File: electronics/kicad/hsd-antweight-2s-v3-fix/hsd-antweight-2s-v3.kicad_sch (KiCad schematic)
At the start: 13 parts, among them J10 ACCESSORY_POWER, J2 ESP32-C3_RIGHT, J4 BATTERY_2S_7V4, J5 MOTOR_LEFT, J6 MOTOR_RIGHT, J9 ESP32_RIGHT_BREAKOUT, SW1 MAIN_POWER, U1 ESP32-C3_LEFT, U2 DRV8833_BREAKOUT, U3 5V_BUCK_BOOST

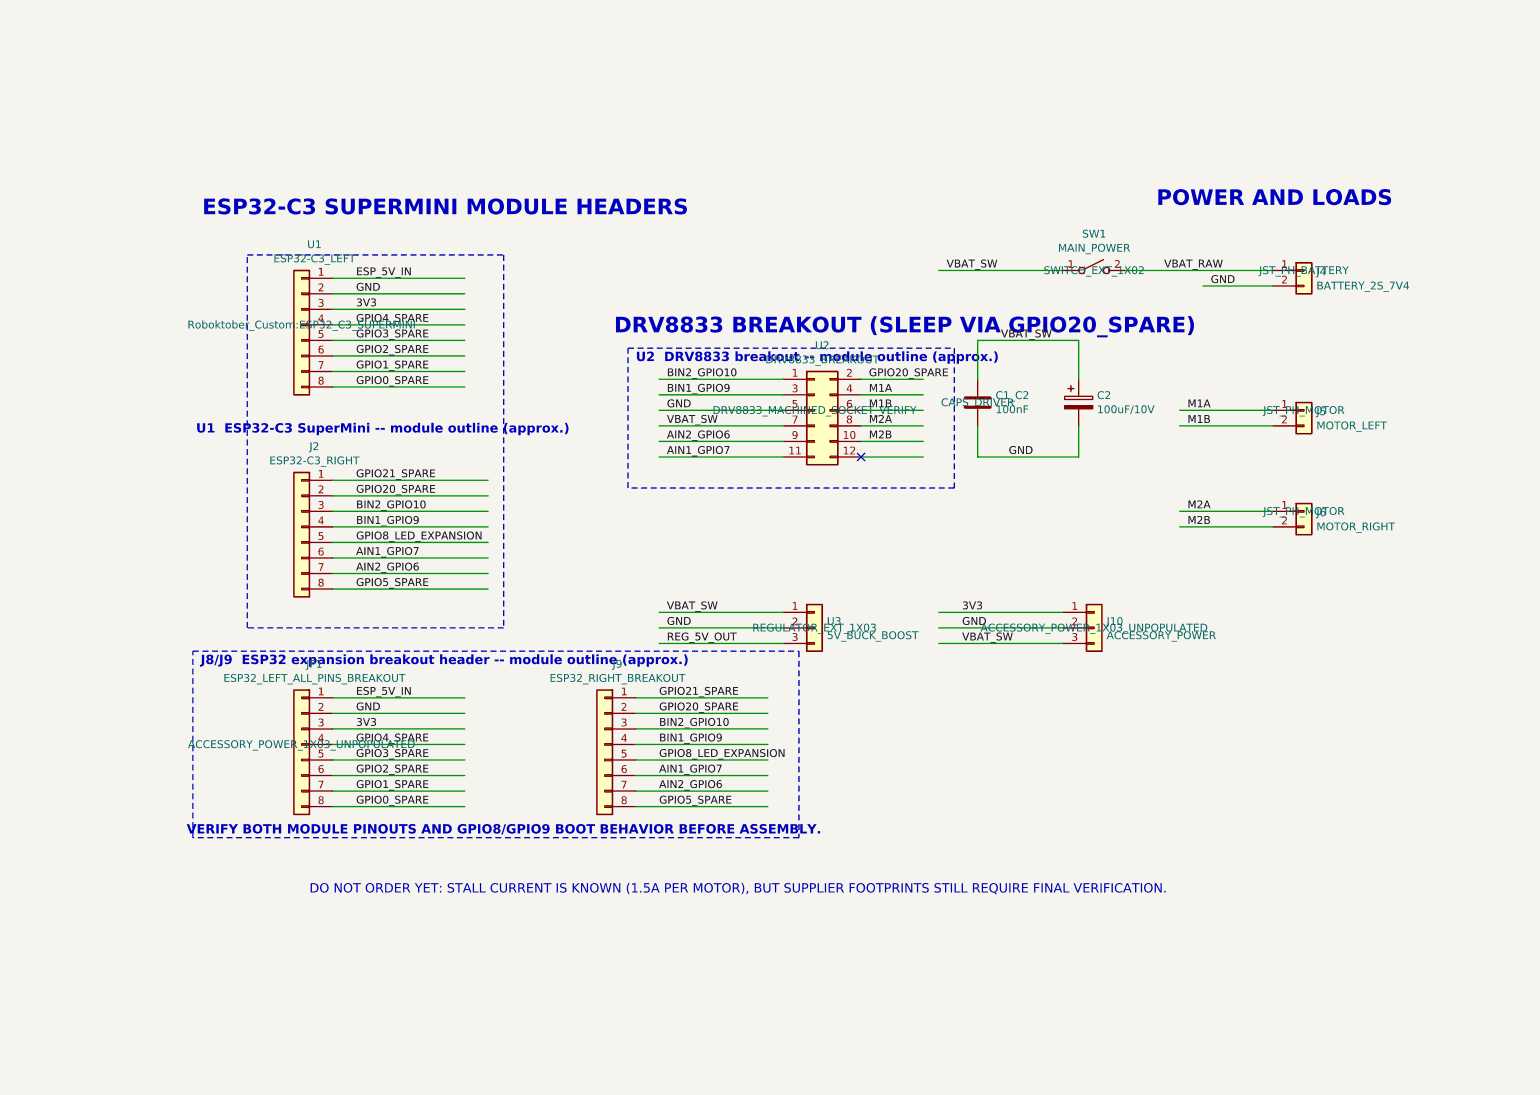
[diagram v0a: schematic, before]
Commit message: Align Wallie design notes with 1S default power architecture
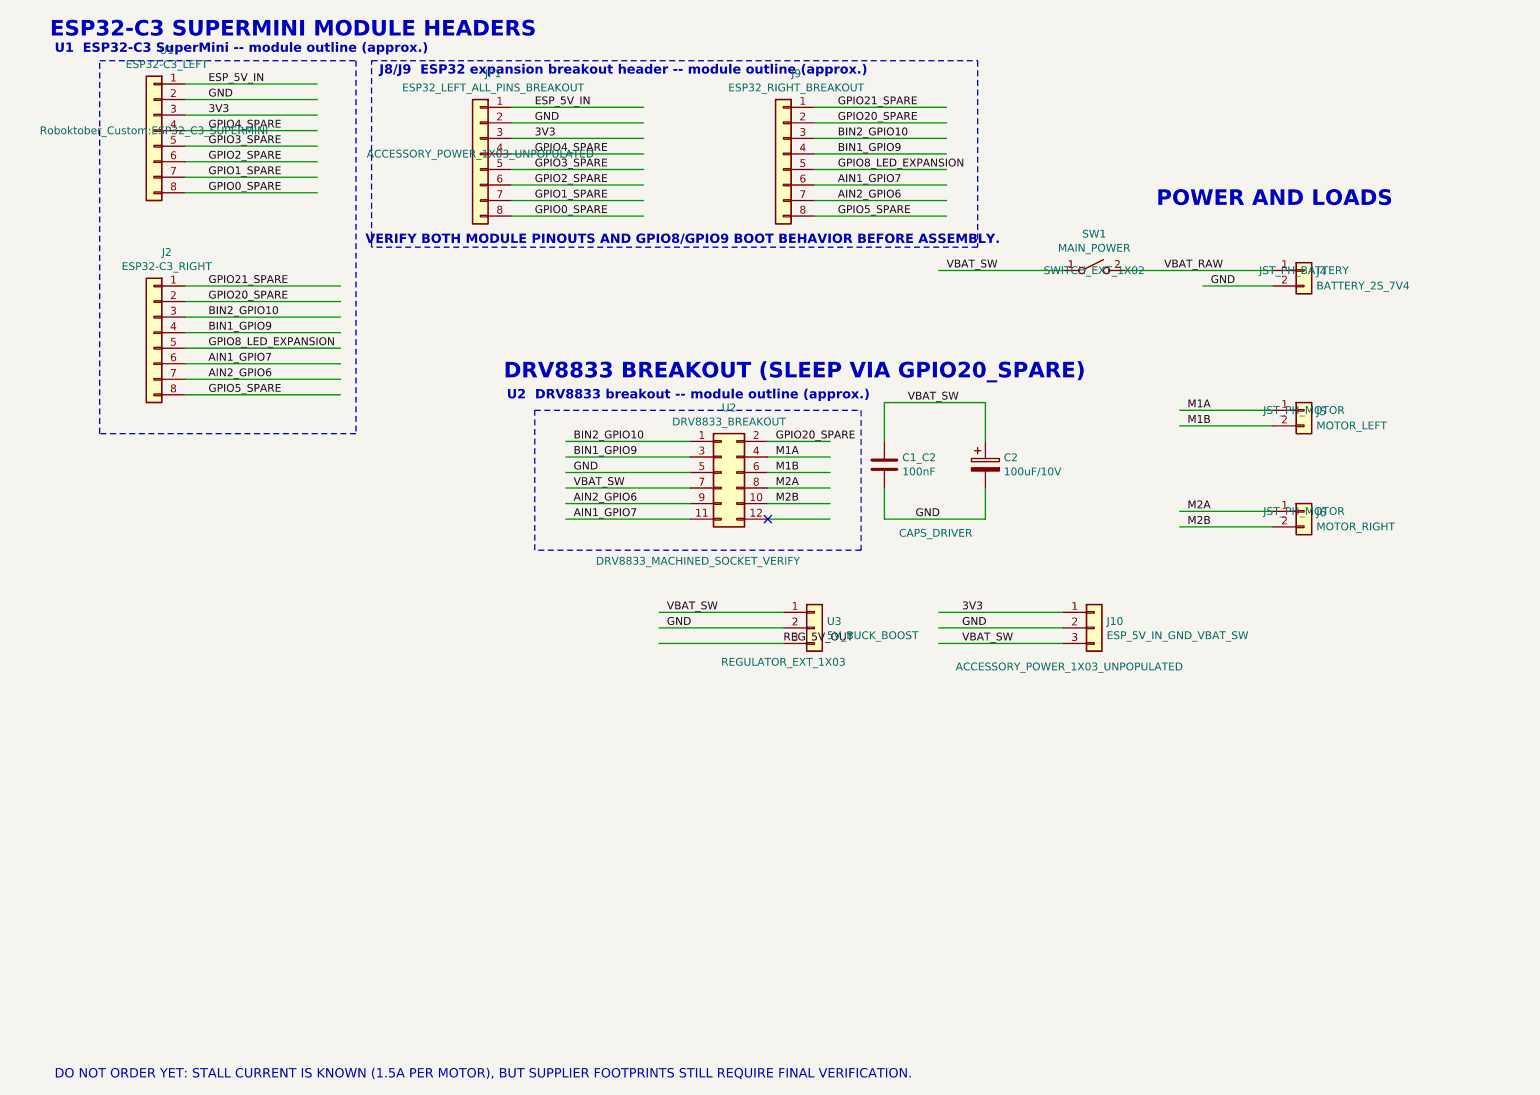
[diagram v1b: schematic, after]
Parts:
- J10: value ACCESSORY_POWER -> ESP_5V_IN_GND_VBAT_SW
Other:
- moved on the sheet: C1_C2, C2, J2, J9, JP1, U1, U2

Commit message: Fix PCB DRC: power trace width and silkscreen overlap
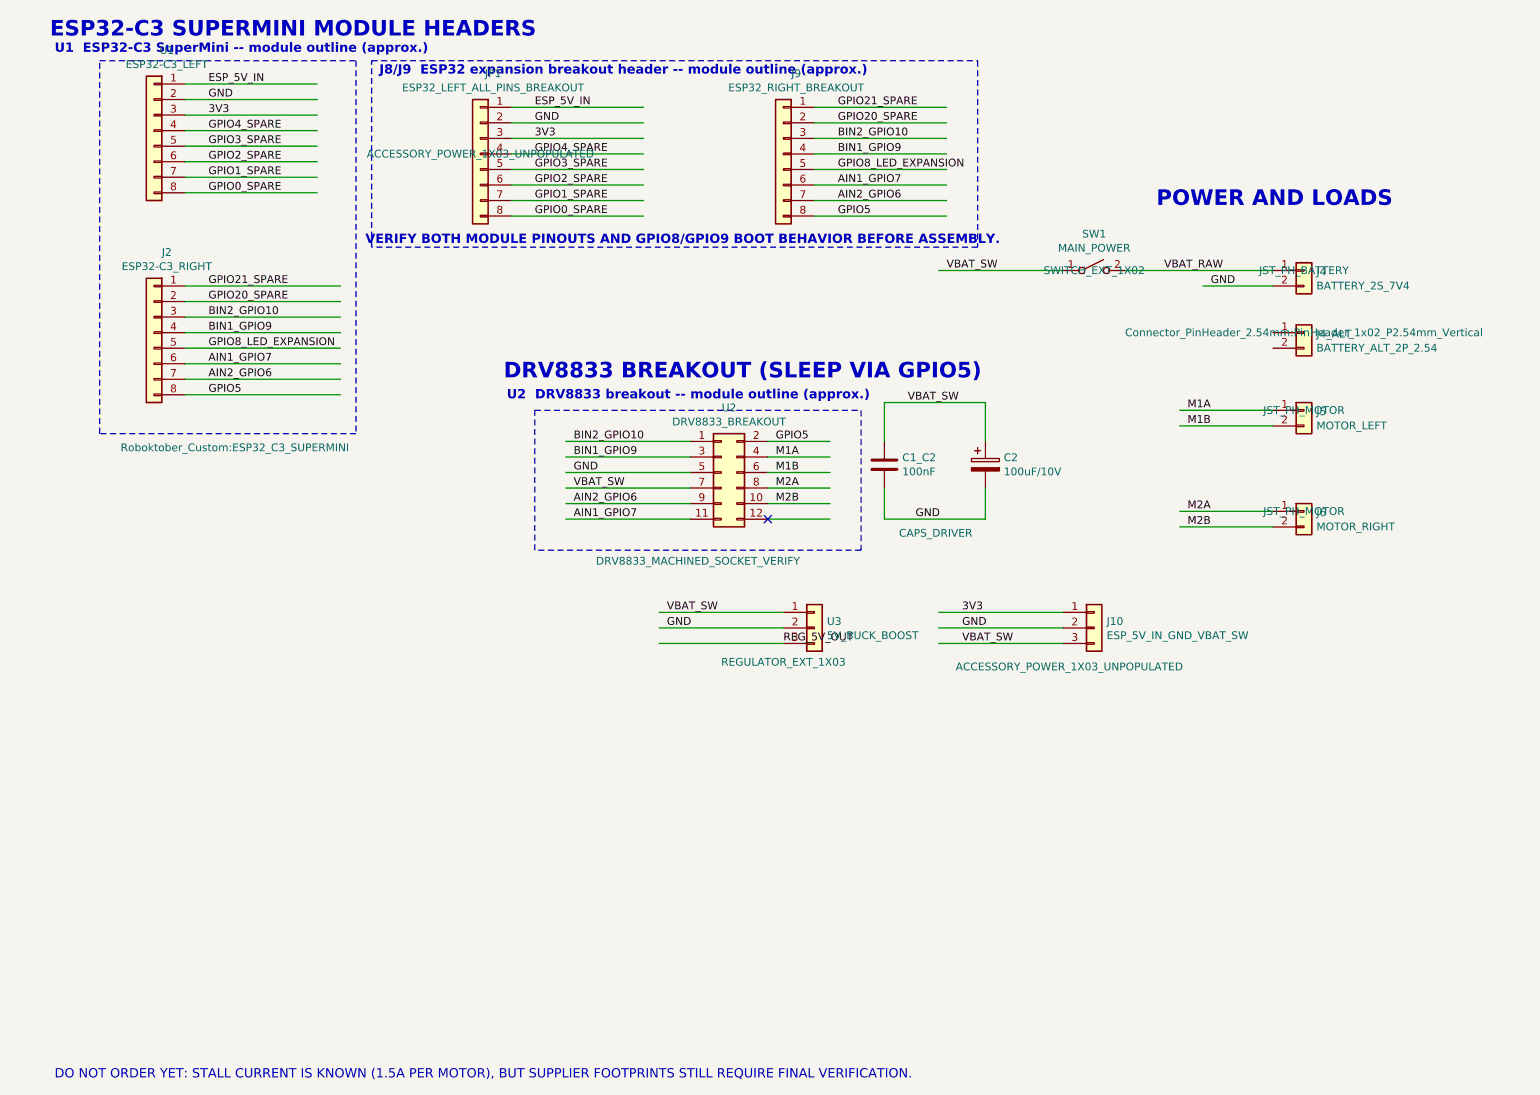
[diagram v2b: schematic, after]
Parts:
- added J4_ALT: BATTERY_ALT_2P_2.54, Connector_PinHeader_2.54mm:PinHeader_1x02_P2.54mm_Vertical, symbol Connector_Generic:Conn_01x02
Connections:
- net GPIO20_SPARE: no longer U2.2 (Pin_2)
- net GPIO5_SPARE renamed GPIO5
- net GPIO5: now also U2.2 (Pin_2)
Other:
- note added: "DRV8833 BREAKOUT (SLEEP VIA GPIO5)"
- note removed: "DRV8833 BREAKOUT (SLEEP VIA GPIO20_SPARE)"
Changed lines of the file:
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@@
 		(rev "3.0")
 		(company "Hackerspace Drenthe")
-		(comment 1 "ESP32-C3 SuperMini + DRV8833 carrier (nSLEEP wired to GPIO20_SPARE)")
+		(comment 1 "ESP32-C3 SuperMini + DRV8833 carrier (nSLEEP wired to GPIO5)")
 		(comment 2 "N20 600rpm measured max 1.5A per motor (3.0A combined)")
 	)
@@
 		)
 	)
-	(text "DRV8833 BREAKOUT (SLEEP VIA GPIO20_SPARE)"
+	(text "DRV8833 BREAKOUT (SLEEP VIA GPIO5)"
 		(exclude_from_sim no)
 		(at 90.17 80.264 0)
@@
 		)
 	)
-	(label "GPIO5_SPARE"
+	(label "GPIO5"
 		(at 41.91 82.55 0)
 		(effects
@@
 		)
 	)
-	(label "GPIO20_SPARE"
+	(label "GPIO5"
 		(at 134.62 90.17 0)
 		(effects
@@
 		)
 	)
-	(label "GPIO5_SPARE"
+	(label "GPIO5"
 		(at 144.78 53.34 0)
 		(effects
@@
 		)
 		(property "Footprint" "Roboktober_Custom:ESP32_C3_SUPERMINI"
-			(at 33.02 39.37 0)
+			(at 46.228 91.186 0)
 			(effects
 				(font
@@
 					(unit 1)
 				)
+			)
+		)
+	)
+	(symbol
+		(lib_id "Connector_Generic:Conn_01x02")
+		(at 220.98 72.39 0)
+		(unit 1)
+		(exclude_from_sim no)
+		(in_bom yes)
+		(on_board yes)
+		(dnp no)
+		(uuid "00000000-0000-0000-0000-000020000004_ALT")
+		(property "Reference" "J4_ALT"
+			(at 223.012 72.5932 0)
+			(effects
+				(font
+					(size 1.27 1.27)
+				)
+				(justify left)
+			)
+		)
+		(property "Value" "BATTERY_ALT_2P_2.54"
+			(at 223.012 74.9046 0)
+			(effects
+				(font
+					(size 1.27 1.27)
+				)
+				(justify left)
+			)
+		)
+		(property "Footprint" "Connector_PinHeader_2.54mm:PinHeader_1x02_P2.54mm_Vertical"
+			(at 220.98 72.39 0)
+			(effects
+				(font
+					(size 1.27 1.27)
+				)
+			)
+		)
+		(property "Datasheet" ""
+			(at 220.98 72.39 0)
+			(effects
+				(font
+					(size 1.27 1.27)
+				)
+			)
+		)
+		(property "Description" ""
+			(at 220.98 72.39 0)
+			(effects
+				(font
+					(size 1.27 1.27)
+				)
+			)
+		)
+		(pin "2"
+		)
+		(pin "1"
+		)
+		(instances
+			(project "hsd-antweight-2s-v3"
+				(path "/f81be06f-f81b-406f-b81b-e06ff81be06f"
+					(reference "J4_ALT")
+					(unit 1)
+				)
